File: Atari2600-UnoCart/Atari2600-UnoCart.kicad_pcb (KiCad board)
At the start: 2 copper layers, 41.3 x 45.7 mm, 23 parts, among them J1 A2600 card edge, J2 Micro_SD_Card, J3 PROG, U1 STM32F407VGTx, U2 SPX3819M5-L-3-3, U3 XC6206PxxxMR

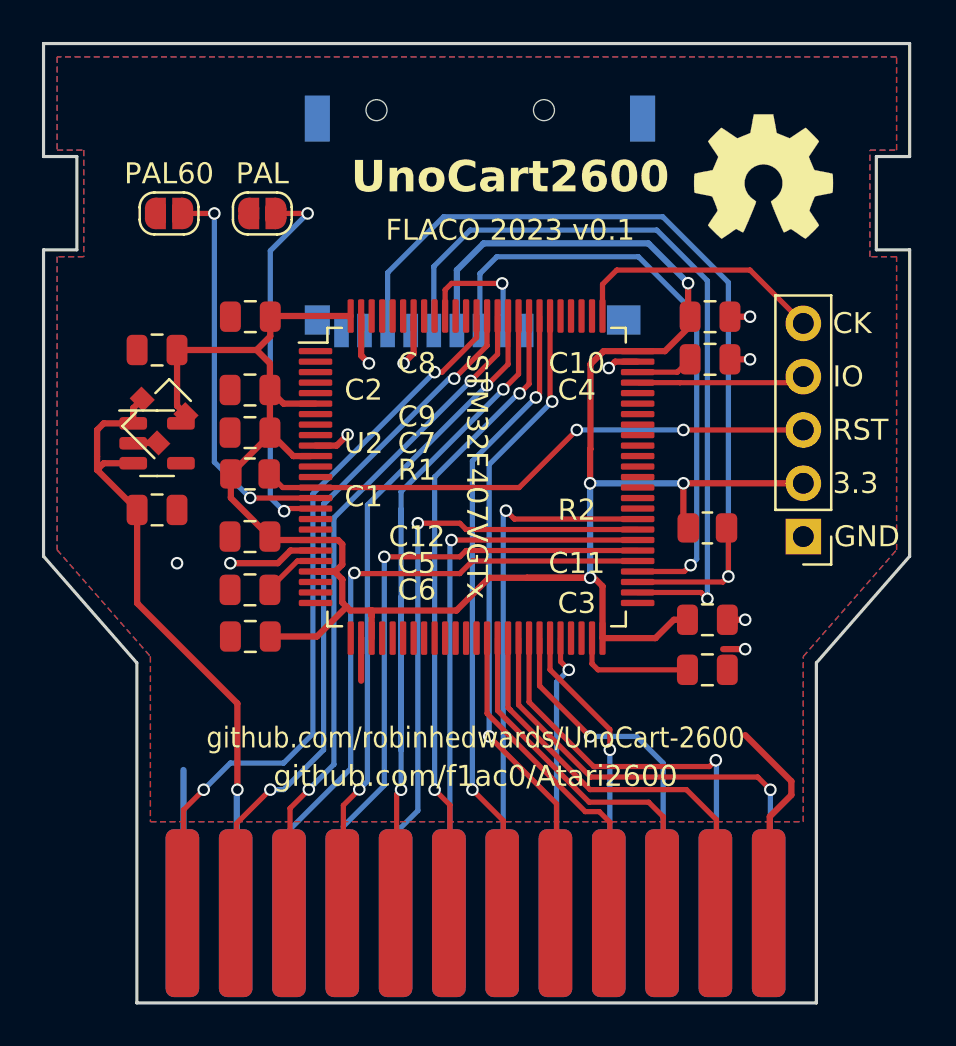
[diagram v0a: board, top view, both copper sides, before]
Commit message: Addition of Atari2600-SECAM2RGB ; update license of Atari2600-UnoCart and README.
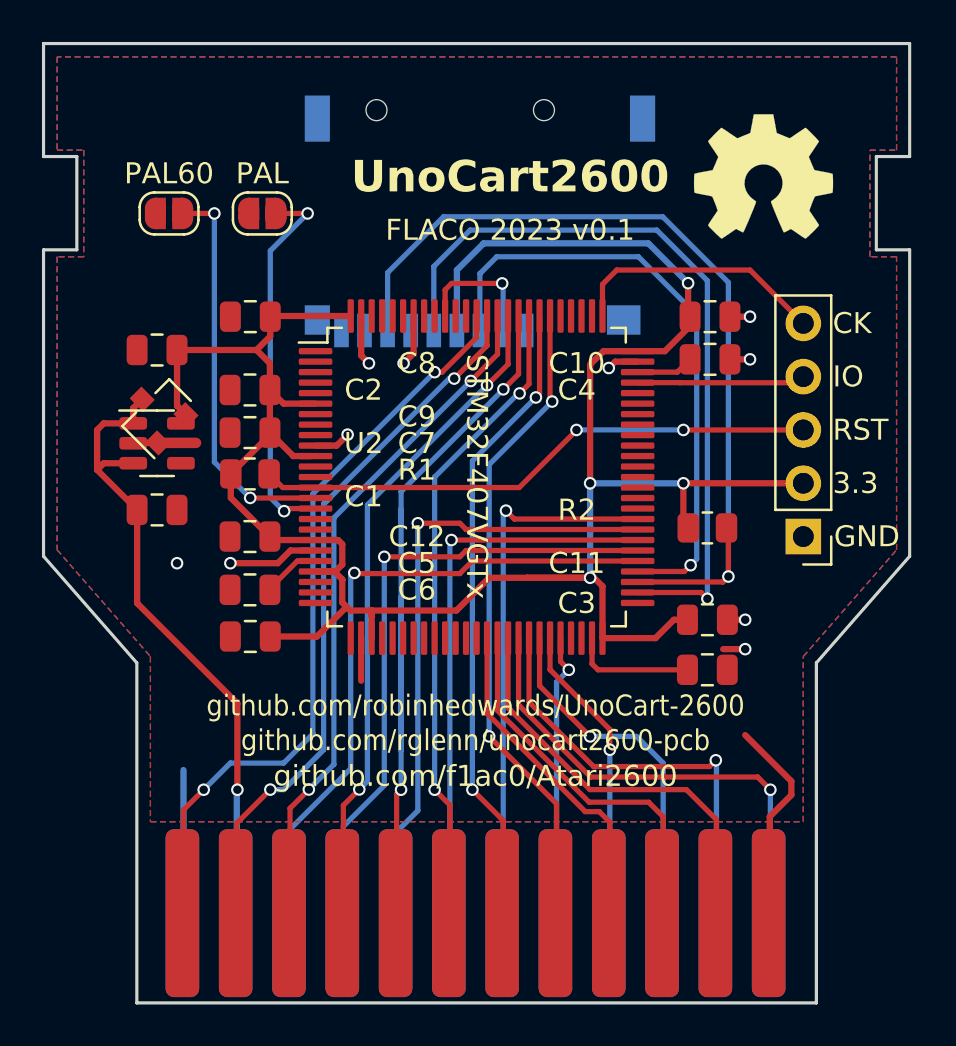
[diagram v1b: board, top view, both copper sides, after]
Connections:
- net +3V3 renamed +3.3V
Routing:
- net GND: track 35.3 -> 37.1 mm
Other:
- rule pad_to_mask_clearance: 0.2 -> 0.038
- board text added: "Copyright of original design Randy Glenn 2021. Modifications by FLACO 2023. This documentation describes Open Hardware and is licensed under the CERN OHL v. 1.2. You may redistribute and modify this documentation under the terms of the CERN OHL v.1.2. (http://ohwr.org/cernohl). This documentation is distributed WITHOUT ANY EXPRESS OR IMPLIED WARRANTY, INCLUDING OF MERCHANTABILITY, SATISFACTORY QU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"
- board text added: "github.com/rglenn/unocart2600-pcb"
